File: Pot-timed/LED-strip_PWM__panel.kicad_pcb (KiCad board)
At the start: 2 copper layers, 160 x 100 mm, 14 parts

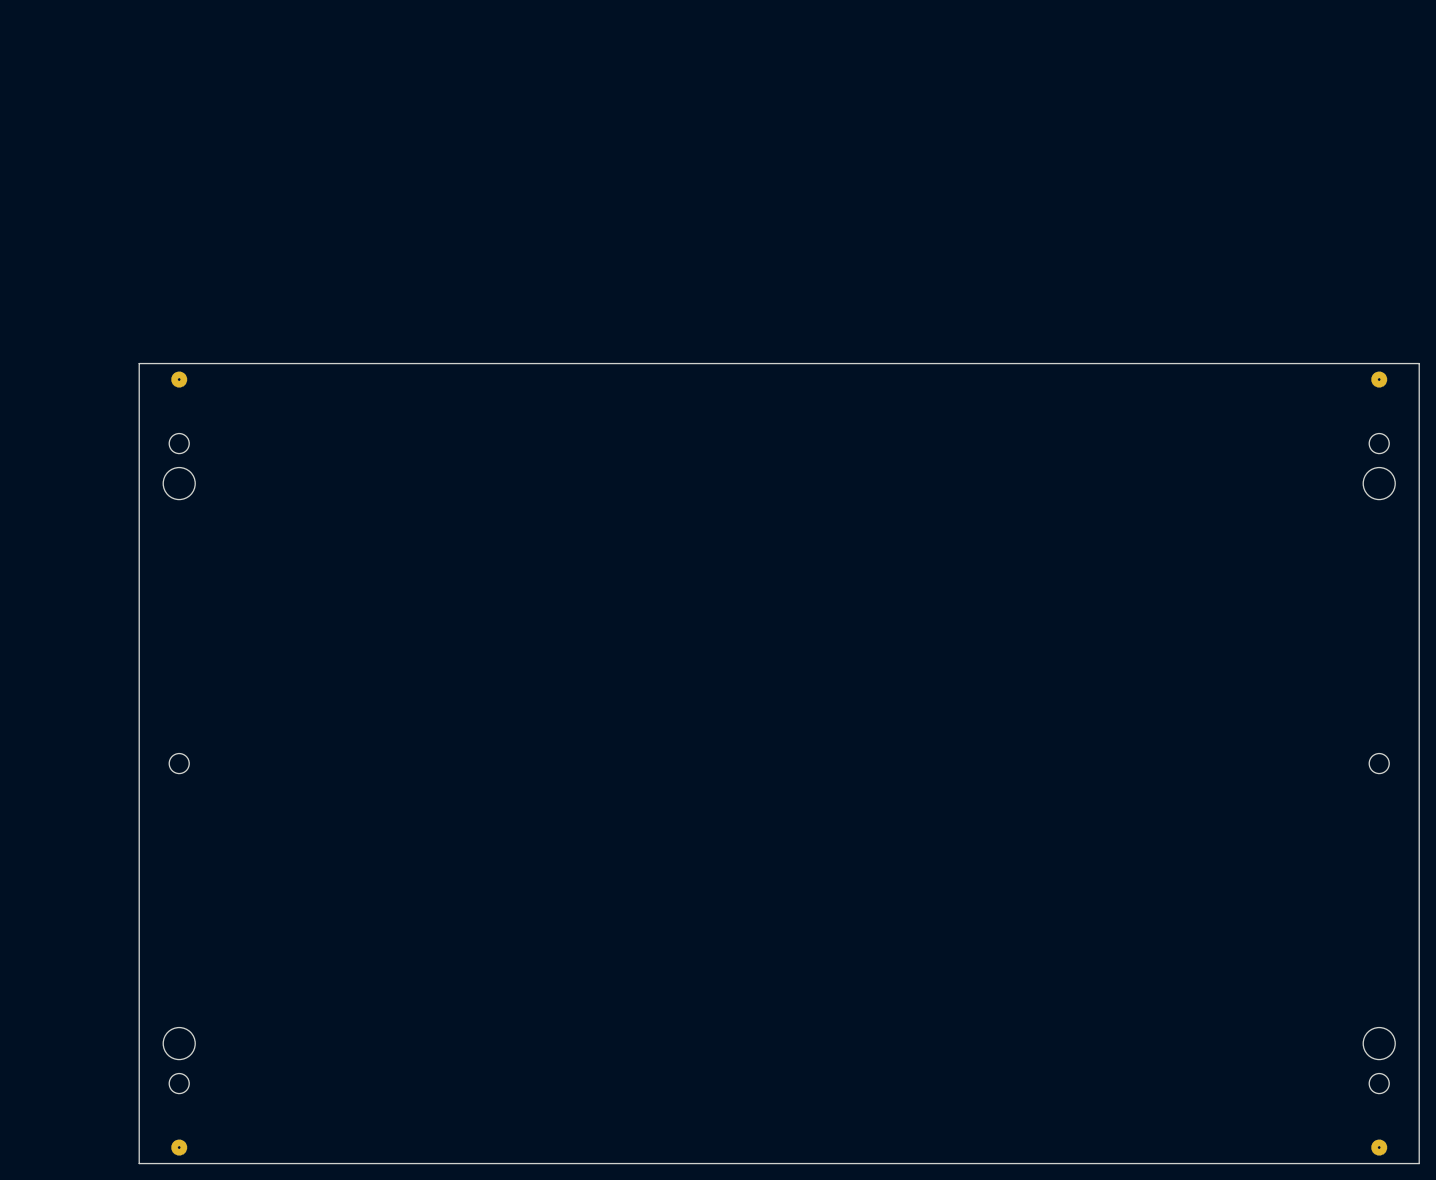
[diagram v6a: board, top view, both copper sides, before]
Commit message: Pot-timed (panel): resized to 10cm x 10cm.
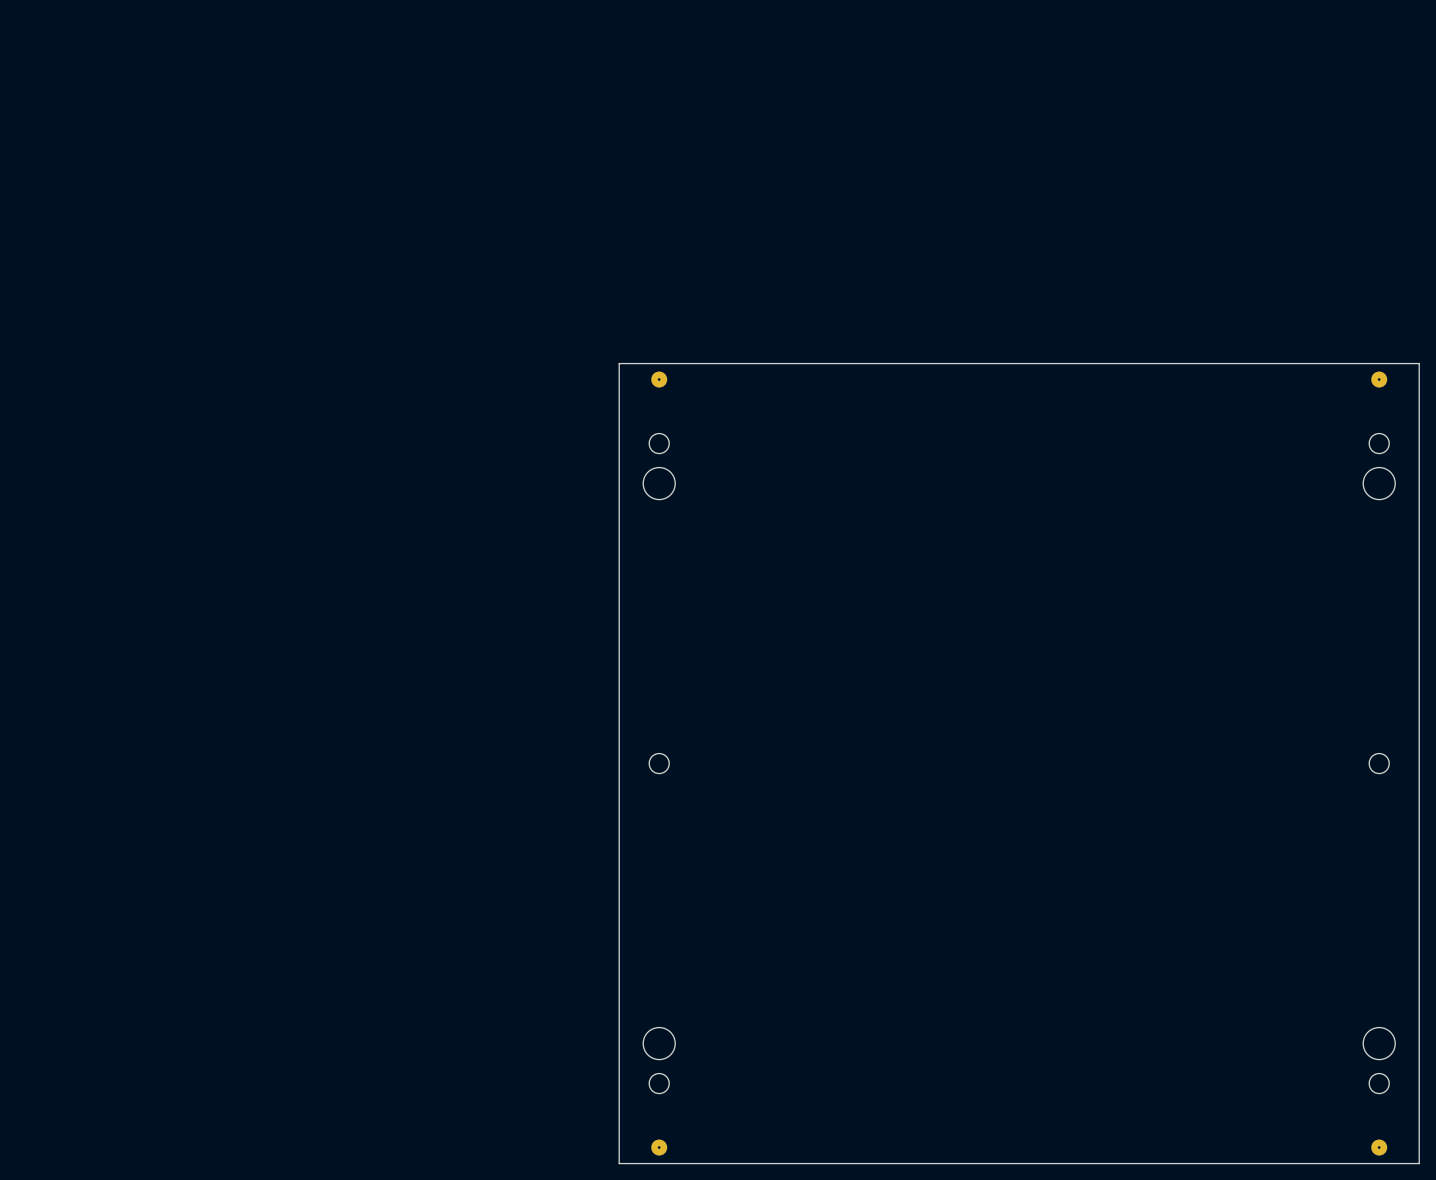
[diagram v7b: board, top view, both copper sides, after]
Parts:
- moved 1PIN 60.0 mm to (165.0, 180.0)
- moved 1PIN 60.0 mm to (165.0, 84.0)
- moved BH1 60.0 mm to (165.0, 97.0)
- moved BH2 60.0 mm to (165.0, 167.0)
- moved SM1 60.0 mm to (165.0, 92.0)
- moved SM2 60.0 mm to (165.0, 132.0)
- moved SM3 60.0 mm to (165.0, 172.0)
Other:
- board size 160 x 100 mm -> 100 x 100 mm
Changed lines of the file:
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@@
-(kicad_pcb (version 3) (host pcbnew "(2013-06-28 BZR 4228)-testing")
+(kicad_pcb (version 3) (host pcbnew "(2013-07-14 BZR 4242)-testing")
   (general
     (links 0)
     (no_connects 0)
-    (area 99.924999 80.1646 260.075001 183.5814)
+    (area 159.924999 80.1646 260.075001 183.5814)
     (thickness 1.6002)
-    (drawings 22)
+    (drawings 16)
     (tracks 0)
     (zones 0)
@@
   )
   (module 1pin (layer Front)
-    (at 105 132)
+    (at 165 132)
     (descr "module 1 pin (ou trou mecanique de percage)")
     (tags DEV)
@@
   )
   (module 1pin (layer Front)
-    (at 105 92)
+    (at 165 92)
     (descr "module 1 pin (ou trou mecanique de percage)")
     (tags DEV)
@@
   )
   (module 1pin (layer Front)
-    (at 105 172)
+    (at 165 172)
     (descr "module 1 pin (ou trou mecanique de percage)")
     (tags DEV)
@@
   )
   (module 1pin (layer Front)
-    (at 105 167)
+    (at 165 167)
     (descr "module 1 pin (ou trou mecanique de percage)")
     (tags DEV)
@@
   )
   (module 1pin (layer Front)
-    (at 105 97)
+    (at 165 97)
     (descr "module 1 pin (ou trou mecanique de percage)")
     (tags DEV)
@@
   )
   (module 1pin (layer Front)
-    (at 105 180)
+    (at 165 180)
     (descr "module 1 pin (ou trou mecanique de percage)")
     (tags DEV)
@@
   )
   (module 1pin (layer Front)
-    (at 105 84)
+    (at 165 84)
     (descr "module 1 pin (ou trou mecanique de percage)")
     (tags DEV)
@@
     )
   )
-  (gr_line (start 260 177.975) (end 100 177.975) (angle 90) (layer Eco2.User) (width 0.1))
-  (gr_line (start 100 86.025) (end 260 86.025) (angle 90) (layer Eco2.User) (width 0.1))
-  (gr_line (start 207.5 82) (end 207.5 182) (angle 90) (layer Eco2.User) (width 0.1))
-  (gr_line (start 196.5 82) (end 196.5 182) (angle 90) (layer Eco2.User) (width 0.1))
-  (gr_line (start 240.5 82) (end 240.5 182) (angle 90) (layer Eco2.User) (width 0.1))
-  (gr_line (start 229.5 82) (end 229.5 182) (angle 90) (layer Eco2.User) (width 0.1))
-  (gr_line (start 218.5 82) (end 218.5 182) (angle 90) (layer Eco2.User) (width 0.1))
-  (gr_line (start 152.5 82) (end 152.5 182) (angle 90) (layer Eco2.User) (width 0.1))
-  (gr_line (start 163.5 82) (end 163.5 182) (angle 90) (layer Eco2.User) (width 0.1))
-  (gr_line (start 185.5 82) (end 185.5 182) (angle 90) (layer Eco2.User) (width 0.1))
-  (gr_line (start 174.5 82) (end 174.5 182) (angle 90) (layer Eco2.User) (width 0.1))
-  (gr_line (start 130.5 82) (end 130.5 182) (angle 90) (layer Eco2.User) (width 0.1))
-  (gr_line (start 141.5 82) (end 141.5 182) (angle 90) (layer Eco2.User) (width 0.1))
-  (gr_line (start 119.5 82) (end 119.5 182) (angle 90) (layer Eco2.User) (width 0.1))
-  (gr_line (start 251.5 182) (end 251.5 82) (angle 90) (layer Eco2.User) (width 0.1))
-  (gr_line (start 108.5 82) (end 108.5 182) (angle 90) (layer Eco2.User) (width 0.1))
-  (gr_line (start 260 147.325) (end 100 147.325) (angle 90) (layer Eco2.User) (width 0.1))
-  (gr_line (start 100 116.675) (end 260 116.675) (angle 90) (layer Eco2.User) (width 0.1))
-  (gr_line (start 260 182) (end 100 182) (angle 90) (layer Edge.Cuts) (width 0.15))
-  (gr_line (start 100 82) (end 100 182) (angle 90) (layer Edge.Cuts) (width 0.15))
-  (gr_line (start 260 82) (end 100 82) (angle 90) (layer Edge.Cuts) (width 0.15))
+  (gr_line (start 260 177.975) (end 160 177.975) (angle 90) (layer Eco2.User) (width 0.1))
+  (gr_line (start 260 86.025) (end 160 86.025) (angle 90) (layer Eco2.User) (width 0.1))
+  (gr_line (start 204.5 82) (end 204.5 182) (angle 90) (layer Eco2.User) (width 0.1))
+  (gr_line (start 193.5 82) (end 193.5 182) (angle 90) (layer Eco2.User) (width 0.1))
+  (gr_line (start 237.5 82) (end 237.5 182) (angle 90) (layer Eco2.User) (width 0.1))
+  (gr_line (start 226.5 82) (end 226.5 182) (angle 90) (layer Eco2.User) (width 0.1))
+  (gr_line (start 215.5 82) (end 215.5 182) (angle 90) (layer Eco2.User) (width 0.1))
+  (gr_line (start 182.5 82) (end 182.5 182) (angle 90) (layer Eco2.User) (width 0.1))
+  (gr_line (start 171.5 82) (end 171.5 182) (angle 90) (layer Eco2.User) (width 0.1))
+  (gr_line (start 248.5 182) (end 248.5 82) (angle 90) (layer Eco2.User) (width 0.1))
+  (gr_line (start 260 147.325) (end 160 147.325) (angle 90) (layer Eco2.User) (width 0.1))
+  (gr_line (start 260 116.675) (end 160 116.675) (angle 90) (layer Eco2.User) (width 0.1))
+  (gr_line (start 260 182) (end 160 182) (angle 90) (layer Edge.Cuts) (width 0.15))
+  (gr_line (start 160 82) (end 160 182) (angle 90) (layer Edge.Cuts) (width 0.15))
+  (gr_line (start 260 82) (end 160 82) (angle 90) (layer Edge.Cuts) (width 0.15))
   (gr_line (start 260 182) (end 260 82) (angle 90) (layer Edge.Cuts) (width 0.15))
 )

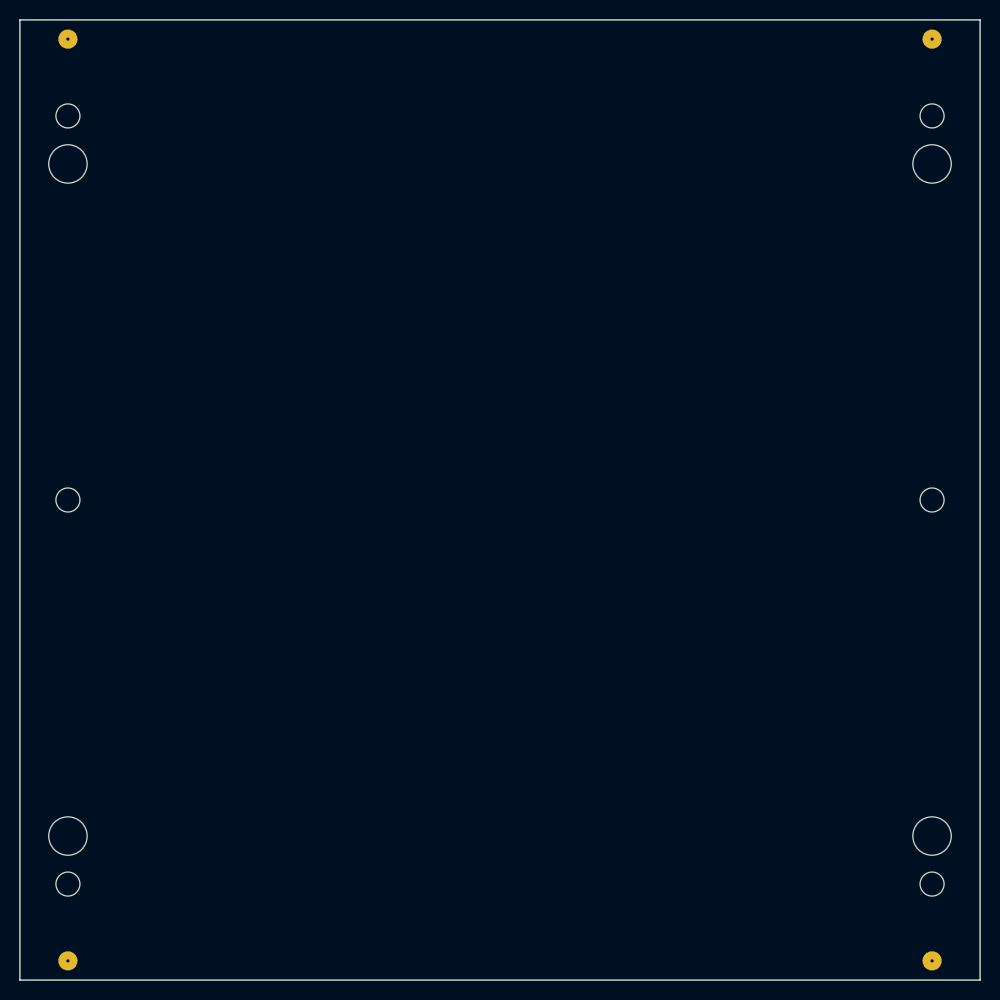
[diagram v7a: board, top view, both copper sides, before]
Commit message: Pot-timed (panel): tweaked to 9.9cm x 10cm.
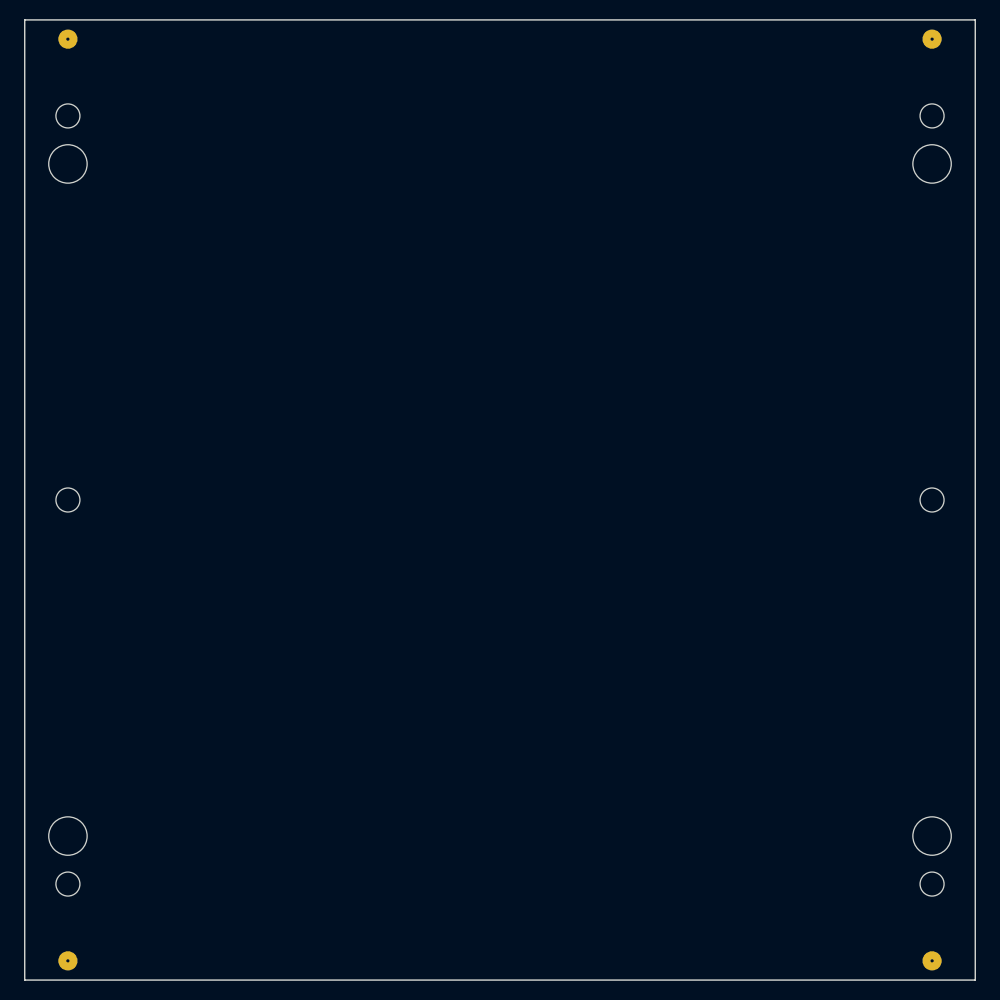
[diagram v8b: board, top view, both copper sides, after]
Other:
- board size 100 x 100 mm -> 99 x 100 mm
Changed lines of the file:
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@@
     (links 0)
     (no_connects 0)
-    (area 159.924999 80.1646 260.075001 183.5814)
+    (area 160.424999 80.1646 259.575001 183.5814)
     (thickness 1.6002)
     (drawings 16)
@@
     (mod_text_size 0.8 0.8)
     (mod_text_width 0.2)
-    (pad_size 4 2.5)
-    (pad_drill 1.2)
+    (pad_size 2 2)
+    (pad_drill 0.333)
     (pad_to_mask_clearance 0)
     (pad_to_paste_clearance_ratio -0.06)
@@
     )
   )
-  (gr_line (start 260 177.975) (end 160 177.975) (angle 90) (layer Eco2.User) (width 0.1))
-  (gr_line (start 260 86.025) (end 160 86.025) (angle 90) (layer Eco2.User) (width 0.1))
+  (gr_line (start 259.5 82) (end 259.5 182) (angle 90) (layer Edge.Cuts) (width 0.15))
+  (gr_line (start 160.5 182) (end 160.5 82) (angle 90) (layer Edge.Cuts) (width 0.15))
+  (gr_line (start 259.5 177.975) (end 160.5 177.975) (angle 90) (layer Eco2.User) (width 0.1))
+  (gr_line (start 259.5 86.025) (end 160.5 86.025) (angle 90) (layer Eco2.User) (width 0.1))
   (gr_line (start 204.5 82) (end 204.5 182) (angle 90) (layer Eco2.User) (width 0.1))
   (gr_line (start 193.5 82) (end 193.5 182) (angle 90) (layer Eco2.User) (width 0.1))
@@
   (gr_line (start 171.5 82) (end 171.5 182) (angle 90) (layer Eco2.User) (width 0.1))
   (gr_line (start 248.5 182) (end 248.5 82) (angle 90) (layer Eco2.User) (width 0.1))
-  (gr_line (start 260 147.325) (end 160 147.325) (angle 90) (layer Eco2.User) (width 0.1))
-  (gr_line (start 260 116.675) (end 160 116.675) (angle 90) (layer Eco2.User) (width 0.1))
-  (gr_line (start 260 182) (end 160 182) (angle 90) (layer Edge.Cuts) (width 0.15))
-  (gr_line (start 160 82) (end 160 182) (angle 90) (layer Edge.Cuts) (width 0.15))
-  (gr_line (start 260 82) (end 160 82) (angle 90) (layer Edge.Cuts) (width 0.15))
-  (gr_line (start 260 182) (end 260 82) (angle 90) (layer Edge.Cuts) (width 0.15))
+  (gr_line (start 259.5 147.325) (end 160.5 147.325) (angle 90) (layer Eco2.User) (width 0.1))
+  (gr_line (start 259.5 116.675) (end 160.5 116.675) (angle 90) (layer Eco2.User) (width 0.1))
+  (gr_line (start 259.5 182) (end 160.5 182) (angle 90) (layer Edge.Cuts) (width 0.15))
+  (gr_line (start 259.5 82) (end 160.5 82) (angle 90) (layer Edge.Cuts) (width 0.15))
 )
